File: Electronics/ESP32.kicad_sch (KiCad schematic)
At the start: 19 parts, among them Q1 BSH108, Q2 BSH108, Q3 BSH108, Q4 BSH108, Q5 RSC002P03, Q6 RSC002P03, U7 ESP32-WROOM-32D

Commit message: made some changes
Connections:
- net 5V Switch 1: now also U7.4 (SENSOR_VP); no longer U7.28 (IO17)
- net Bat I: now also U7.7 (IO35); no longer U7.37 (IO23)
- net Bat V: now also U7.6 (IO34); no longer U7.10 (IO25)
- net Line Sensor 3: now also U7.29 (IO5); no longer U7.24 (IO2)
- net Line Sensor 5: now also U7.28 (IO17)
- net Line Sensor LED: now also U7.37 (IO23); no longer U7.26 (IO4)
- net Motor PWM3: no longer U7.7 (IO35)
- net Motor PWM4: now also U7.10 (IO25); no longer U7.6 (IO34)
- net Pen Servo: now also U7.5 (SENSOR_VN); no longer U7.29 (IO5)
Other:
- moved on the sheet: C11, C12

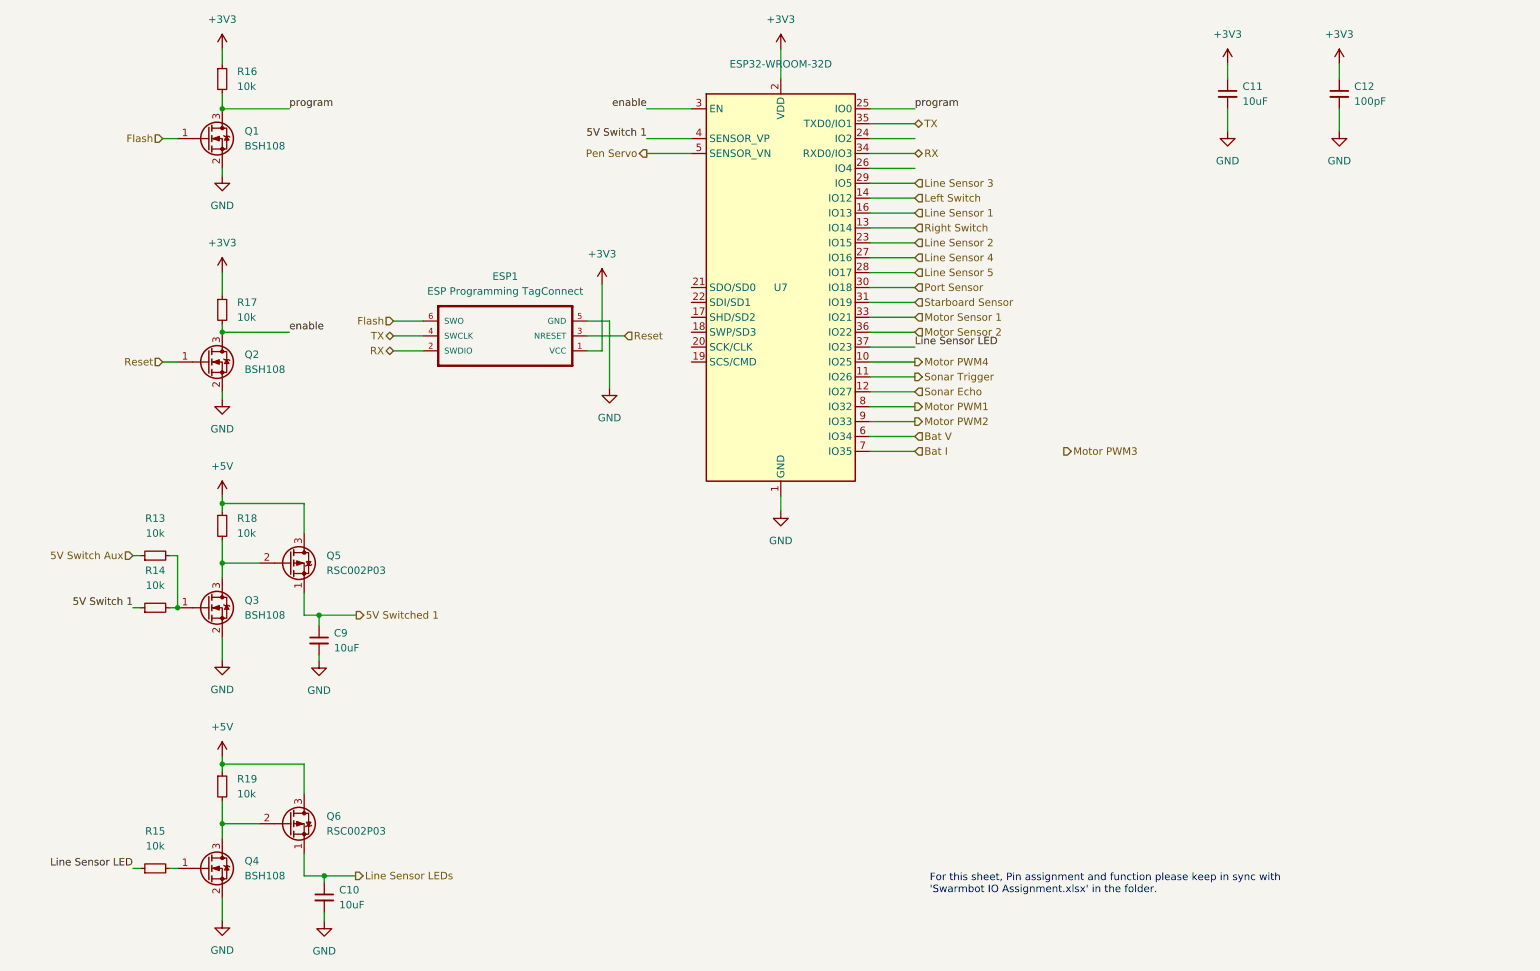
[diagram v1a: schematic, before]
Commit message: added bom
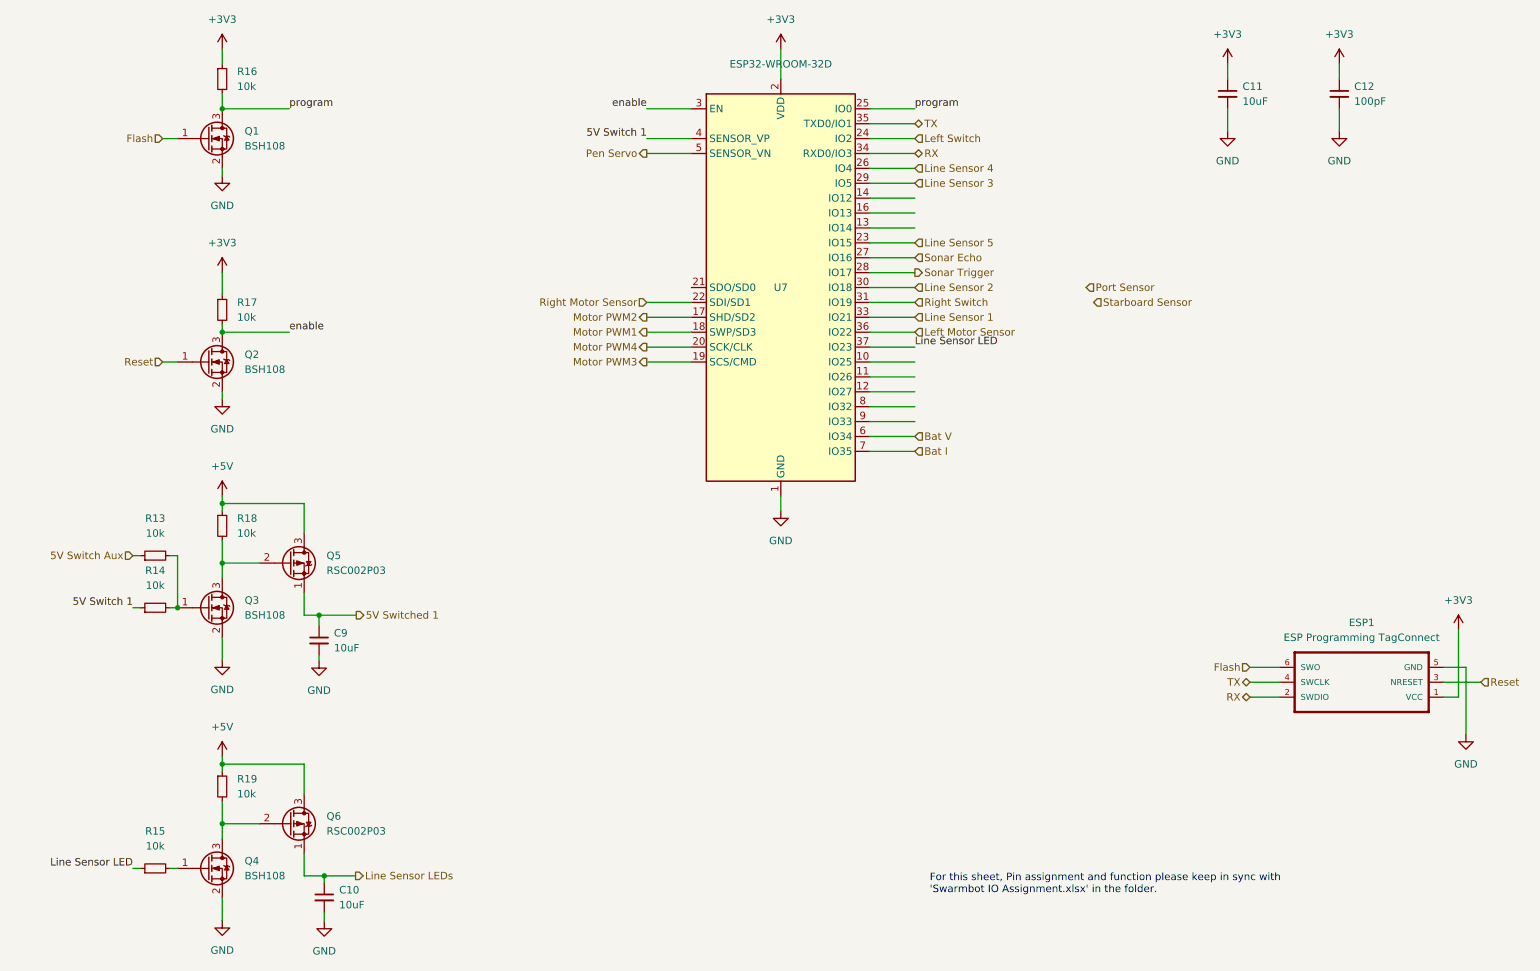
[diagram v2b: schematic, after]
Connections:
- net Motor Sensor 1 is gone; now on net Line Sensor 1: U7.33 (IO21)
- net Left Switch: now also U7.24 (IO2); no longer U7.14 (IO12)
- net Line Sensor 1: no longer U7.16 (IO13)
- net Line Sensor 2: now also U7.30 (IO18); no longer U7.23 (IO15)
- net Line Sensor 4: now also U7.26 (IO4); no longer U7.27 (IO16)
- net Line Sensor 5: now also U7.23 (IO15); no longer U7.28 (IO17)
- net Motor PWM1: now also U7.18 (SWP/SD3); no longer U7.8 (IO32)
- net Motor PWM2: now also U7.17 (SHD/SD2); no longer U7.9 (IO33)
- net Motor PWM3: now also U7.19 (SCS/CMD)
- net Motor PWM4: now also U7.20 (SCK/CLK); no longer U7.10 (IO25)
- net Port Sensor: no longer U7.30 (IO18)
- net Right Switch: now also U7.31 (IO19); no longer U7.13 (IO14)
- net Sonar Echo: now also U7.27 (IO16); no longer U7.12 (IO27)
- net Sonar Trigger: now also U7.28 (IO17); no longer U7.11 (IO26)
- net Starboard Sensor: no longer U7.31 (IO19)
- net Right Motor Sensor: now reaches U7.22 (SDI/SD1)
- net Motor Sensor 2 renamed Left Motor Sensor
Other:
- moved on the sheet: ESP1

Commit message: del backups
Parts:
- renumbered C9 to C10, C10 to C11, C11 to C12, C12 to C13, R13 to R17, R14 to R18, R15 to R19, R16 to R20, R17 to R21, R18 to R22, R19 to R23, U7 to U9
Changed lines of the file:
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@@
   (symbol (lib_id "power:+3V3") (at 64.77 34.29 0) (unit 1)
     (in_bom yes) (on_board yes) (fields_autoplaced)
-    (property "Reference" "#PWR020" (id 0) (at 64.77 38.1 0)
+    (property "Reference" "#PWR011" (id 0) (at 64.77 38.1 0)
       (effects (font (size 1.27 1.27)) hide)
     )
@@
   (symbol (lib_id "power:+3V3") (at 64.77 72.39 0) (unit 1)
     (in_bom yes) (on_board yes) (fields_autoplaced)
-    (property "Reference" "#PWR022" (id 0) (at 64.77 76.2 0)
+    (property "Reference" "#PWR013" (id 0) (at 64.77 76.2 0)
       (effects (font (size 1.27 1.27)) hide)
     )
@@
   (symbol (lib_id "power:+5V") (at 64.77 110.49 0) (unit 1)
     (in_bom yes) (on_board yes) (fields_autoplaced)
-    (property "Reference" "#PWR024" (id 0) (at 64.77 114.3 0)
+    (property "Reference" "#PWR015" (id 0) (at 64.77 114.3 0)
       (effects (font (size 1.27 1.27)) hide)
     )
@@
   (symbol (lib_id "power:+5V") (at 64.77 154.94 0) (unit 1)
     (in_bom yes) (on_board yes) (fields_autoplaced)
-    (property "Reference" "#PWR026" (id 0) (at 64.77 158.75 0)
+    (property "Reference" "#PWR017" (id 0) (at 64.77 158.75 0)
       (effects (font (size 1.27 1.27)) hide)
     )
@@
   (symbol (lib_id "power:+3V3") (at 160.02 34.29 0) (unit 1)
     (in_bom yes) (on_board yes) (fields_autoplaced)
-    (property "Reference" "#PWR034" (id 0) (at 160.02 38.1 0)
+    (property "Reference" "#PWR021" (id 0) (at 160.02 38.1 0)
       (effects (font (size 1.27 1.27)) hide)
     )
@@
   (symbol (lib_id "power:+3V3") (at 236.22 36.83 0) (unit 1)
     (in_bom yes) (on_board yes) (fields_autoplaced)
-    (property "Reference" "#PWR030" (id 0) (at 236.22 40.64 0)
+    (property "Reference" "#PWR023" (id 0) (at 236.22 40.64 0)
       (effects (font (size 1.27 1.27)) hide)
     )
@@
   (symbol (lib_id "power:+3V3") (at 255.27 36.83 0) (unit 1)
     (in_bom yes) (on_board yes) (fields_autoplaced)
-    (property "Reference" "#PWR032" (id 0) (at 255.27 40.64 0)
+    (property "Reference" "#PWR025" (id 0) (at 255.27 40.64 0)
       (effects (font (size 1.27 1.27)) hide)
     )
@@
   (symbol (lib_id "power:+3V3") (at 275.59 133.35 0) (unit 1)
     (in_bom yes) (on_board yes) (fields_autoplaced)
-    (property "Reference" "#PWR036" (id 0) (at 275.59 137.16 0)
+    (property "Reference" "#PWR027" (id 0) (at 275.59 137.16 0)
       (effects (font (size 1.27 1.27)) hide)
     )
@@
   (symbol (lib_id "power:GND") (at 64.77 55.88 0) (unit 1)
     (in_bom yes) (on_board yes) (fields_autoplaced)
-    (property "Reference" "#PWR021" (id 0) (at 64.77 62.23 0)
+    (property "Reference" "#PWR012" (id 0) (at 64.77 62.23 0)
       (effects (font (size 1.27 1.27)) hide)
     )
@@
   (symbol (lib_id "power:GND") (at 64.77 93.98 0) (unit 1)
     (in_bom yes) (on_board yes) (fields_autoplaced)
-    (property "Reference" "#PWR023" (id 0) (at 64.77 100.33 0)
+    (property "Reference" "#PWR014" (id 0) (at 64.77 100.33 0)
       (effects (font (size 1.27 1.27)) hide)
     )
@@
   (symbol (lib_id "power:GND") (at 64.77 138.43 0) (unit 1)
     (in_bom yes) (on_board yes) (fields_autoplaced)
-    (property "Reference" "#PWR025" (id 0) (at 64.77 144.78 0)
+    (property "Reference" "#PWR016" (id 0) (at 64.77 144.78 0)
       (effects (font (size 1.27 1.27)) hide)
     )
@@
   (symbol (lib_id "power:GND") (at 64.77 182.88 0) (unit 1)
     (in_bom yes) (on_board yes) (fields_autoplaced)
-    (property "Reference" "#PWR027" (id 0) (at 64.77 189.23 0)
+    (property "Reference" "#PWR018" (id 0) (at 64.77 189.23 0)
       (effects (font (size 1.27 1.27)) hide)
     )
@@
   (symbol (lib_id "power:GND") (at 81.28 138.557 0) (unit 1)
     (in_bom yes) (on_board yes) (fields_autoplaced)
-    (property "Reference" "#PWR028" (id 0) (at 81.28 144.907 0)
+    (property "Reference" "#PWR019" (id 0) (at 81.28 144.907 0)
       (effects (font (size 1.27 1.27)) hide)
     )
@@
   (symbol (lib_id "power:GND") (at 82.169 183.007 0) (unit 1)
     (in_bom yes) (on_board yes) (fields_autoplaced)
-    (property "Reference" "#PWR029" (id 0) (at 82.169 189.357 0)
+    (property "Reference" "#PWR020" (id 0) (at 82.169 189.357 0)
       (effects (font (size 1.27 1.27)) hide)
     )
@@
   (symbol (lib_id "power:GND") (at 160.02 113.03 0) (unit 1)
     (in_bom yes) (on_board yes) (fields_autoplaced)
-    (property "Reference" "#PWR035" (id 0) (at 160.02 119.38 0)
+    (property "Reference" "#PWR022" (id 0) (at 160.02 119.38 0)
       (effects (font (size 1.27 1.27)) hide)
     )
@@
   (symbol (lib_id "power:GND") (at 236.22 48.26 0) (unit 1)
     (in_bom yes) (on_board yes)
-    (property "Reference" "#PWR031" (id 0) (at 236.22 54.61 0)
+    (property "Reference" "#PWR024" (id 0) (at 236.22 54.61 0)
       (effects (font (size 1.27 1.27)) hide)
     )
@@
   (symbol (lib_id "power:GND") (at 255.27 48.26 0) (unit 1)
     (in_bom yes) (on_board yes)
-    (property "Reference" "#PWR033" (id 0) (at 255.27 54.61 0)
+    (property "Reference" "#PWR026" (id 0) (at 255.27 54.61 0)
       (effects (font (size 1.27 1.27)) hide)
     )
@@
   (symbol (lib_id "power:GND") (at 276.86 151.13 0) (unit 1)
     (in_bom yes) (on_board yes) (fields_autoplaced)
-    (property "Reference" "#PWR037" (id 0) (at 276.86 157.48 0)
+    (property "Reference" "#PWR028" (id 0) (at 276.86 157.48 0)
       (effects (font (size 1.27 1.27)) hide)
     )
@@
   (symbol (lib_id "Device:R_Small") (at 53.34 120.65 90) (unit 1)
     (in_bom yes) (on_board yes) (fields_autoplaced)
-    (property "Reference" "R13" (id 0) (at 53.34 114.3 90))
+    (property "Reference" "R17" (id 0) (at 53.34 114.3 90))
     (property "Value" "10k" (id 1) (at 53.34 116.84 90))
     (property "Footprint" "Resistor_SMD:R_0805_2012Metric_Pad1.20x1.40mm_HandSolder" (id 2) (at 53.34 120.65 0)
@@
   (symbol (lib_id "Device:R_Small") (at 53.34 129.54 90) (unit 1)
     (in_bom yes) (on_board yes) (fields_autoplaced)
-    (property "Reference" "R14" (id 0) (at 53.34 123.19 90))
+    (property "Reference" "R18" (id 0) (at 53.34 123.19 90))
     (property "Value" "10k" (id 1) (at 53.34 125.73 90))
     (property "Footprint" "Resistor_SMD:R_0805_2012Metric_Pad1.20x1.40mm_HandSolder" (id 2) (at 53.34 129.54 0)
@@
   (symbol (lib_id "Device:R_Small") (at 53.34 173.99 90) (unit 1)
     (in_bom yes) (on_board yes) (fields_autoplaced)
-    (property "Reference" "R15" (id 0) (at 53.34 167.64 90))
+    (property "Reference" "R19" (id 0) (at 53.34 167.64 90))
     (property "Value" "10k" (id 1) (at 53.34 170.18 90))
     (property "Footprint" "Resistor_SMD:R_0805_2012Metric_Pad1.20x1.40mm_HandSolder" (id 2) (at 53.34 173.99 0)
@@
   (symbol (lib_id "Device:R_Small") (at 64.77 39.37 0) (unit 1)
     (in_bom yes) (on_board yes) (fields_autoplaced)
-    (property "Reference" "R16" (id 0) (at 67.31 38.0999 0)
+    (property "Reference" "R20" (id 0) (at 67.31 38.0999 0)
       (effects (font (size 1.27 1.27)) (justify left))
     )
@@
   (symbol (lib_id "Device:R_Small") (at 64.77 78.74 0) (unit 1)
     (in_bom yes) (on_board yes) (fields_autoplaced)
-    (property "Reference" "R17" (id 0) (at 67.31 77.4699 0)
+    (property "Reference" "R21" (id 0) (at 67.31 77.4699 0)
       (effects (font (size 1.27 1.27)) (justify left))
     )
@@
   (symbol (lib_id "Device:R_Small") (at 64.77 115.57 0) (unit 1)
     (in_bom yes) (on_board yes) (fields_autoplaced)
-    (property "Reference" "R18" (id 0) (at 67.31 114.2999 0)
+    (property "Reference" "R22" (id 0) (at 67.31 114.2999 0)
       (effects (font (size 1.27 1.27)) (justify left))
     )
@@
   (symbol (lib_id "Device:R_Small") (at 64.77 160.02 0) (unit 1)
     (in_bom yes) (on_board yes) (fields_autoplaced)
-    (property "Reference" "R19" (id 0) (at 67.31 158.7499 0)
+    (property "Reference" "R23" (id 0) (at 67.31 158.7499 0)
       (effects (font (size 1.27 1.27)) (justify left))
     )
@@
   (symbol (lib_id "Device:C_Small") (at 81.28 135.128 0) (unit 1)
     (in_bom yes) (on_board yes) (fields_autoplaced)
-    (property "Reference" "C9" (id 0) (at 83.82 133.8579 0)
+    (property "Reference" "C10" (id 0) (at 83.82 133.8579 0)
       (effects (font (size 1.27 1.27)) (justify left))
     )
@@
   (symbol (lib_id "Device:C_Small") (at 82.169 178.943 0) (unit 1)
     (in_bom yes) (on_board yes) (fields_autoplaced)
-    (property "Reference" "C10" (id 0) (at 84.709 177.6729 0)
+    (property "Reference" "C11" (id 0) (at 84.709 177.6729 0)
       (effects (font (size 1.27 1.27)) (justify left))
     )
@@
   (symbol (lib_id "Device:C_Small") (at 236.22 41.91 0) (unit 1)
     (in_bom yes) (on_board yes) (fields_autoplaced)
-    (property "Reference" "C11" (id 0) (at 238.76 40.6399 0)
+    (property "Reference" "C12" (id 0) (at 238.76 40.6399 0)
       (effects (font (size 1.27 1.27)) (justify left))
     )
@@
   (symbol (lib_id "Device:C_Small") (at 255.27 41.91 0) (unit 1)
     (in_bom yes) (on_board yes) (fields_autoplaced)
-    (property "Reference" "C12" (id 0) (at 257.81 40.6399 0)
+    (property "Reference" "C13" (id 0) (at 257.81 40.6399 0)
       (effects (font (size 1.27 1.27)) (justify left))
     )
@@
   (symbol (lib_id "RF_Module:ESP32-WROOM-32D") (at 160.02 74.93 0) (unit 1)
     (in_bom yes) (on_board yes)
-    (property "Reference" "U7" (id 0) (at 160.02 74.93 0))
+    (property "Reference" "U9" (id 0) (at 160.02 74.93 0))
     (property "Value" "ESP32-WROOM-32D" (id 1) (at 160.02 36.83 0))
     (property "Footprint" "RF_Module:ESP32-WROOM-32" (id 2) (at 160.02 113.03 0)

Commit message: some changes were made
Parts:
- removed C11: 10uF, Capacitor_SMD:C_0805_2012Metric_Pad1.18x1.45mm_HandSolder, symbol Device:C_Small
- removed ESP1: ESP Programming TagConnect, TC2030-IDC:Tag-Connect_TC2030-IDC-NL_2x03_P1.27mm_Vertical, symbol TC2030-IDC:TC2030-IDC
- removed Q4: BSH108, Package_TO_SOT_SMD:SOT-23, symbol Device:Q_NMOS_GSD
- removed Q6: RSC002P03, Package_TO_SOT_SMD:SOT-23, symbol Device:Q_PMOS_SGD
- removed R17, R18, R19, R20, R21, R22, R23: 10k, Resistor_SMD:R_0805_2012Metric_Pad1.20x1.40mm_HandSolder, symbol Device:R_Small
- added R32, R33, R34, R35, R36: 10k, Resistor_SMD:R_0805_2012Metric_Pad1.20x1.40mm_HandSolder, symbol Device:R_Small
- renumbered C10 to C11, Q5 to Q10, Q1 to Q7, Q2 to Q8, Q3 to Q9
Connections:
- net +3V3: now also R34.2, R35.2
- net +5V: now also R36.2
- net 5V Switch 1: now also U9.12 (IO27), R33.2; no longer U9.4 (SENSOR_VP)
- net 5V Switch Aux: now also R32.2
- net Bat I: now also U9.10 (IO25); no longer U9.7 (IO35)
- net Bat V: now also U9.9 (IO33); no longer U9.6 (IO34)
- net Left Motor Sensor: now also U9.33 (IO21); no longer U9.36 (IO22)
- net Left Switch: now also U9.20 (SCK/CLK); no longer U9.24 (IO2)
- net Line Sensor 1: now also U9.31 (IO19); no longer U9.33 (IO21)
- net Line Sensor 2: now also U9.28 (IO17); no longer U9.30 (IO18)
- net Line Sensor 3: now also U9.27 (IO16); no longer U9.29 (IO5)
- net Line Sensor 4: now also U9.22 (SDI/SD1); no longer U9.26 (IO4)
- net Line Sensor 5: now also U9.14 (IO12); no longer U9.23 (IO15)
- net Line Sensor LEDs: now also U9.18 (SWP/SD3)
- net Motor PWM1: now also U9.19 (SCS/CMD); no longer U9.18 (SWP/SD3)
- net Motor PWM3: now also U9.21 (SDO/SD0); no longer U9.19 (SCS/CMD)
- net Motor PWM4: now also U9.23 (IO15); no longer U9.20 (SCK/CLK)
- net Pen Servo: now also U9.36 (IO22); no longer U9.5 (SENSOR_VN)
- net Right Motor Sensor: now also U9.13 (IO14); no longer U9.22 (SDI/SD1)
- net Right Switch: now also U9.30 (IO18); no longer U9.31 (IO19)
- net Sonar Echo: now also U9.24 (IO2); no longer U9.27 (IO16)
- net Sonar Trigger: now also U9.26 (IO4); no longer U9.28 (IO17)
- net enable: now also U9.16 (IO13), R35.1; no longer U9.3 (EN)
- net program: now also R34.1
- net at Q9.1 (G): now also R32.1, R33.1
- net IR_LEDS: now reaches U9.8 (IO32)
- net at Q10.2 (G), Q9.3 (D): now also R36.1
- net Line Sensor LED renamed Top PCB V
- new net Bottom PCB V: U9.29 (IO5)
- new net IR_1: U9.3 (EN)
- new net IR_2: U9.4 (SENSOR_VP)
- new net IR_3: U9.5 (SENSOR_VN)
- new net IR_4: U9.6 (IO34)
- new net IR_5: U9.7 (IO35)
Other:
- added sheet IR LEDS (IR LEDS.kicad_sch)
- added sheet Version of PCB (Version.kicad_sch)
- company: Philip McGaw -> Squashed Fly

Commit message: don't use the enable pingit statusgit status
;
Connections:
- net IR_1: now also U9.4 (SENSOR_VP); no longer U9.3 (EN)
- net IR_2: now also U9.5 (SENSOR_VN); no longer U9.4 (SENSOR_VP)
- net IR_3: no longer U9.5 (SENSOR_VN)
- net Line Sensor 5: now also U9.16 (IO13); no longer U9.14 (IO12)
- net enable: now also U9.3 (EN); no longer U9.16 (IO13)
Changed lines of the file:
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@@
     (comment 1 "Design by Philip McGaw")
   )
+  (junction (at 64.77 121.92) (diameter 0) (color 0 0 0 0))
+  (junction (at 81.28 130.81) (diameter 0) (color 0 0 0 0))
   (junction (at 64.77 82.55) (diameter 0) (color 0 0 0 0))
   (junction (at 57.15 129.54) (diameter 0) (color 0 0 0 0))
-  (junction (at 81.28 130.81) (diameter 0) (color 0 0 0 0))
-  (junction (at 64.77 121.92) (diameter 0) (color 0 0 0 0))
   (junction (at 64.77 111.76) (diameter 0) (color 0 0 0 0))
   (junction (at 64.77 44.45) (diameter 0) (color 0 0 0 0))
@@
     (effects (font (size 1.27 1.27)) (justify right bottom))
   )
-  (label "IR_2" (at 137.16 49.53 180)
-    (effects (font (size 1.27 1.27)) (justify right bottom))
-  )
-  (label "enable" (at 182.88 62.23 0)
-    (effects (font (size 1.27 1.27)) (justify left bottom))
+  (label "IR_2" (at 137.16 52.07 180)
+    (effects (font (size 1.27 1.27)) (justify right bottom))
+  )
+  (label "enable" (at 137.16 44.45 180)
+    (effects (font (size 1.27 1.27)) (justify right bottom))
   )
   (label "IR_LEDS" (at 235.585 90.17 180)
@@
     (effects (font (size 1.27 1.27)) (justify left bottom))
   )
-  (label "IR_1" (at 137.16 44.45 180)
+  (label "IR_1" (at 137.16 49.53 180)
     (effects (font (size 1.27 1.27)) (justify right bottom))
   )
@@
     (effects (font (size 1.27 1.27)) (justify right bottom))
   )
-  (label "IR_3" (at 137.16 52.07 180)
+  (label "IR_3" (at 135.89 66.04 180)
     (effects (font (size 1.27 1.27)) (justify right bottom))
   )
@@
     (effects (font (size 1.27 1.27)) (justify right))
   )
-  (hierarchical_label "Line Sensor 5" (shape input) (at 182.88 59.69 0)
-    (effects (font (size 1.27 1.27)) (justify left))
-  )
+  (hierarchical_label "Line Sensor 5" (shape input) (at 182.88 62.23 0)
+    (effects (font (size 1.27 1.27)) (justify left))
+  )
